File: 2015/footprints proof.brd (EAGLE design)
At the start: 50.5 x 29.2 mm, 2 parts

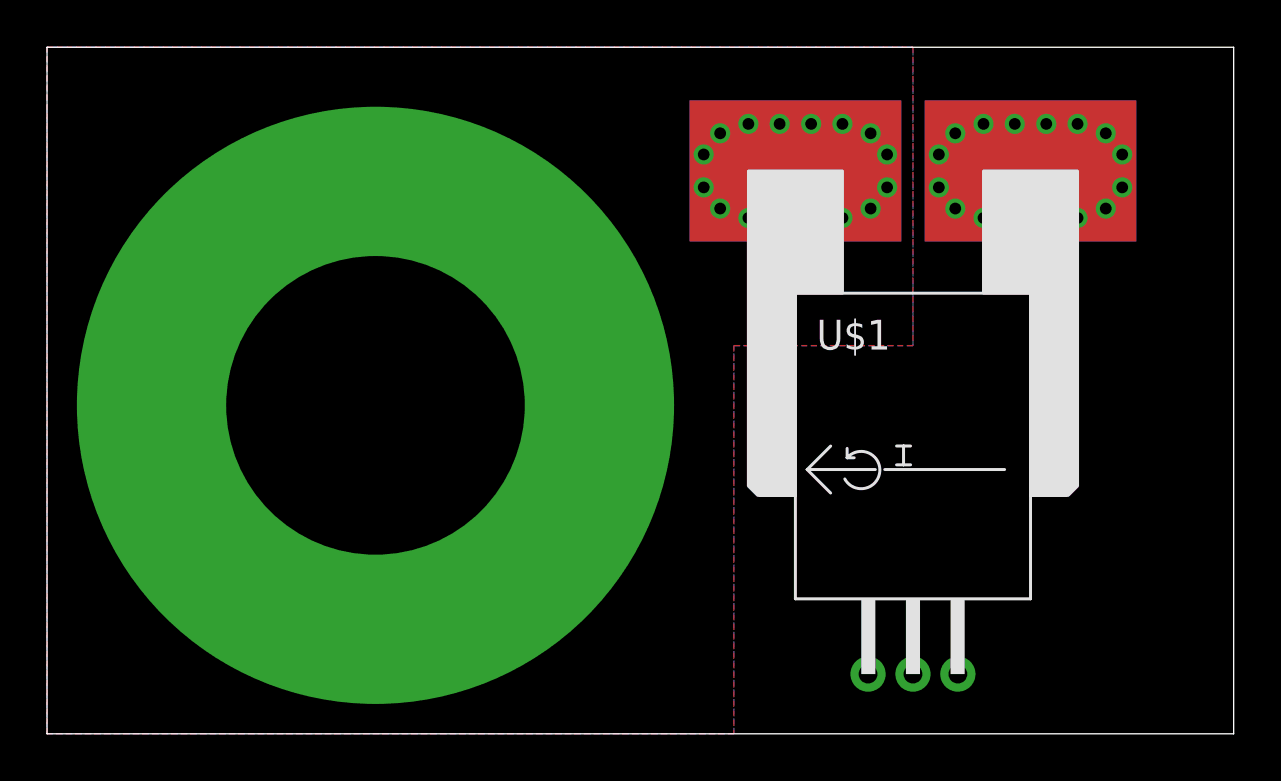
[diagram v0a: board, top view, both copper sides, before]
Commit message: Using fixed parts.
The footprints board should be ordered ASAP
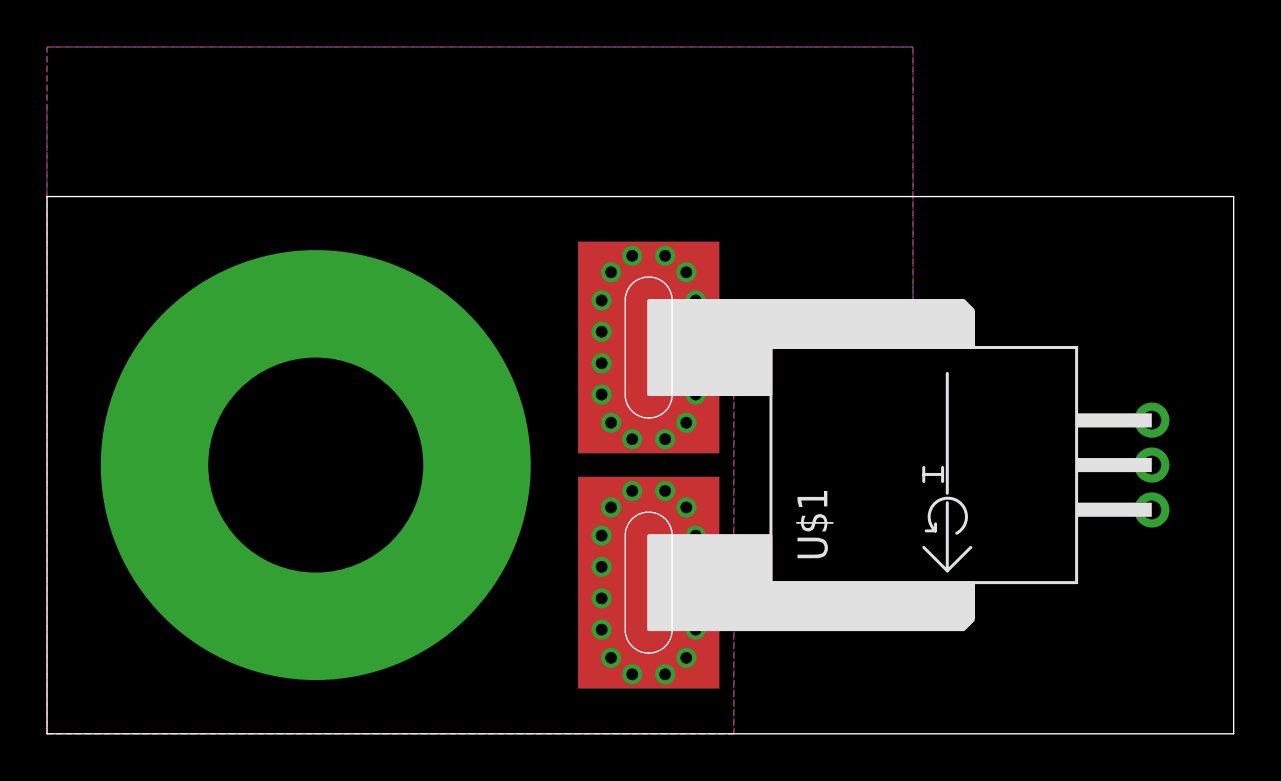
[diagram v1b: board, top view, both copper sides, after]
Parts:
- moved U$1 13.5 mm to (47.0, 11.4), turned to 90 degrees
- moved U$2 3.59 mm to (11.4, 11.4)
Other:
- board size 50.5 x 29.2 mm -> 50.5 x 22.9 mm
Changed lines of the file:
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@@
 <plain>
 <wire x1="0" y1="0" x2="50.47" y2="0" width="0" layer="20"/>
-<wire x1="50.47" y1="0" x2="50.47" y2="29.2" width="0" layer="20"/>
-<wire x1="50.47" y1="29.2" x2="0" y2="29.2" width="0" layer="20"/>
-<wire x1="0" y1="29.2" x2="0" y2="0" width="0" layer="20"/>
+<wire x1="50.47" y1="0" x2="50.47" y2="22.85" width="0" layer="20"/>
+<wire x1="50.47" y1="22.85" x2="0" y2="22.85" width="0" layer="20"/>
+<wire x1="0" y1="22.85" x2="0" y2="0" width="0" layer="20"/>
 </plain>
 <attributes>
@@
 </autorouter>
 <elements>
-<element name="U$1" library="MRDT-2015-BMS" package="PFF_LEADFORM" value="ACS770" x="36.83" y="2.54"/>
-<element name="U$2" library="MRDT-2015-PowerBoard" package="LARGE_TERMINAL_HOLE" value="TERMINAL_HOLE" x="13.97" y="13.97"/>
+<element name="U$1" library="MRDT-2015-BMS" package="PFF_LEADFORM" value="ACS770" x="46.99" y="11.43" rot="R90"/>
+<element name="U$2" library="MRDT-2015-PowerBoard" package="LARGE_TERMINAL_HOLE" value="TERMINAL_HOLE" x="11.43" y="11.43"/>
 </elements>
 <signals>
